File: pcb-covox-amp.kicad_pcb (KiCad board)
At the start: 2 copper layers, 80 x 56 mm, 41 parts, among them J1 DB25, P1 USB, U1 LM386, X1 Amp, X2 Raw

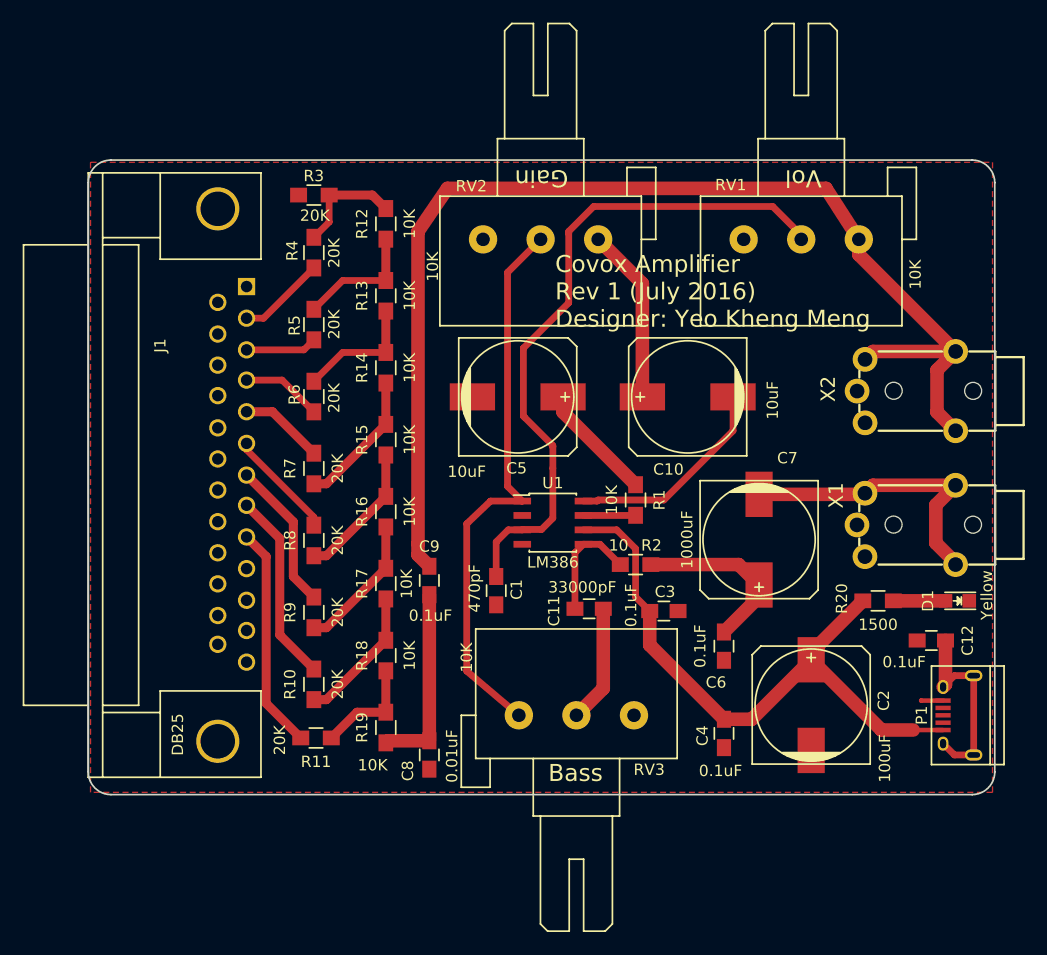
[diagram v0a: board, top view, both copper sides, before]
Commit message: add mounting holes rev 2
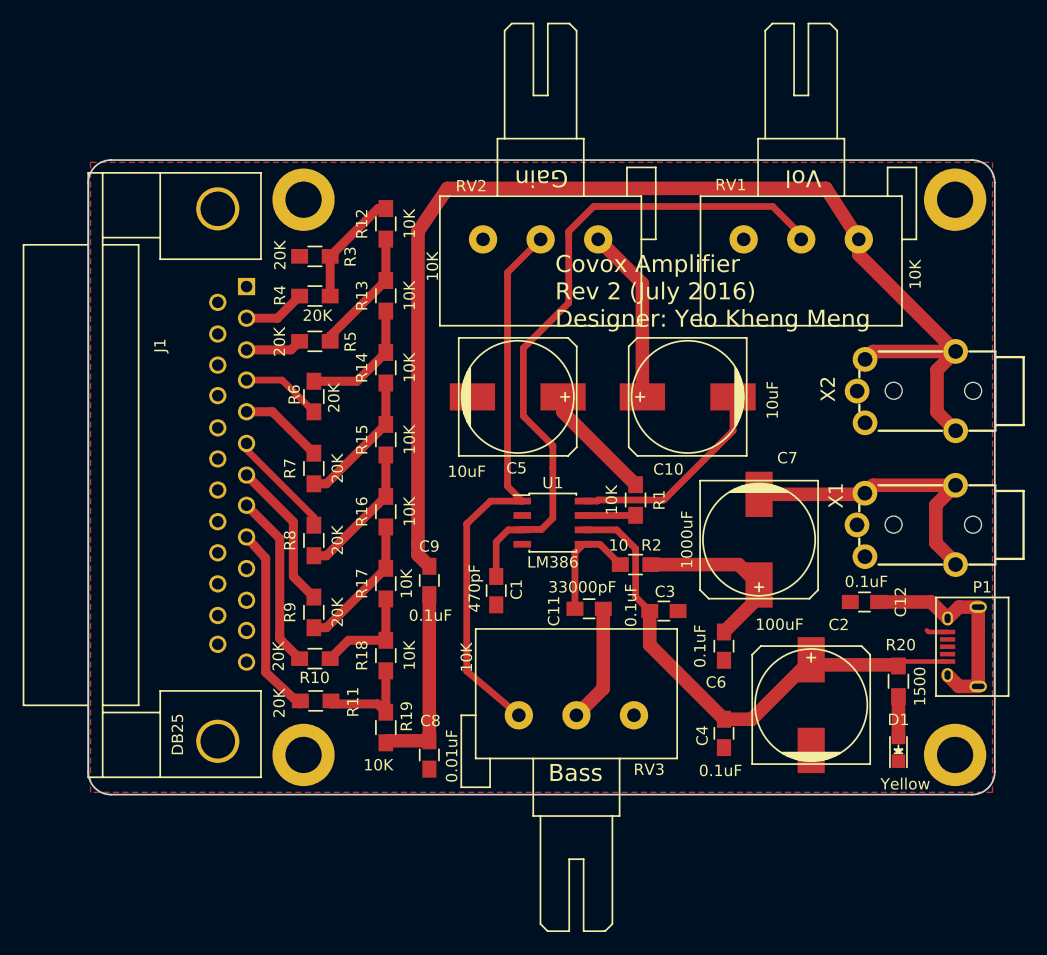
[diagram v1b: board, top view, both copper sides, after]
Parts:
- added MH1: MOUNTHOLE, Mounting_Holes:MountingHole_3.2mm_M3_ISO14580_Pad, F.Cu at (176.5, 89.5)
- added MH2: MOUNTHOLE, Mounting_Holes:MountingHole_3.2mm_M3_ISO14580_Pad, F.Cu at (176.5, 138.5)
- added MH3: MOUNTHOLE, Mounting_Holes:MountingHole_3.2mm_M3_ISO14580_Pad, F.Cu at (119.0, 138.5)
- added MH4: MOUNTHOLE, Mounting_Holes:MountingHole_3.2mm_M3_ISO14580_Pad, F.Cu at (119.0, 89.5)
- moved D1 14.1 mm to (171.5, 138.0), turned to 90 degrees
- moved R20 7.32 mm to (171.5, 132.0), turned to 270 degrees
- moved C12 6.81 mm to (168.5, 125.0)
- moved P1 6.06 mm to (177.4, 128.9)
- moved R3 5.41 mm to (120.0, 94.5)
- moved R4 3.83 mm to (120.0, 98.0), turned to 180 degrees
- moved R11 3.27 mm to (120.1, 133.7)
- moved R10 2.27 mm to (120.0, 130.0), turned to 180 degrees
- moved R5 1.48 mm to (120.0, 102.0), turned to 180 degrees
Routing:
- net +5V: track 54.7 -> 46.4 mm
- net Data7: track 19.7 -> 16.7 mm
- net Net-(R10-Pad1): track 12.2 -> 9.23 mm
- net Net-(C12-Pad2): track 17.6 -> 19.9 mm
- net Data0: track 7.78 -> 5.49 mm
- net Data6: track 16.9 -> 15.5 mm
- net Data1: track 6.30 -> 4.99 mm
- net Net-(D1-Pad2): track 4.60 -> 3.60 mm
- net Net-(R11-Pad1): track 9.40 -> 8.86 mm
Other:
- net class Default: trace_width 1.2 -> 0.4
- board text added: "Covox Amplifier Rev 2 (July 2016) Designer: Yeo Kheng Meng"
- board text removed: "Covox Amplifier Rev 1 (July 2016) Designer: Yeo Kheng Meng"

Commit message: update db25 package
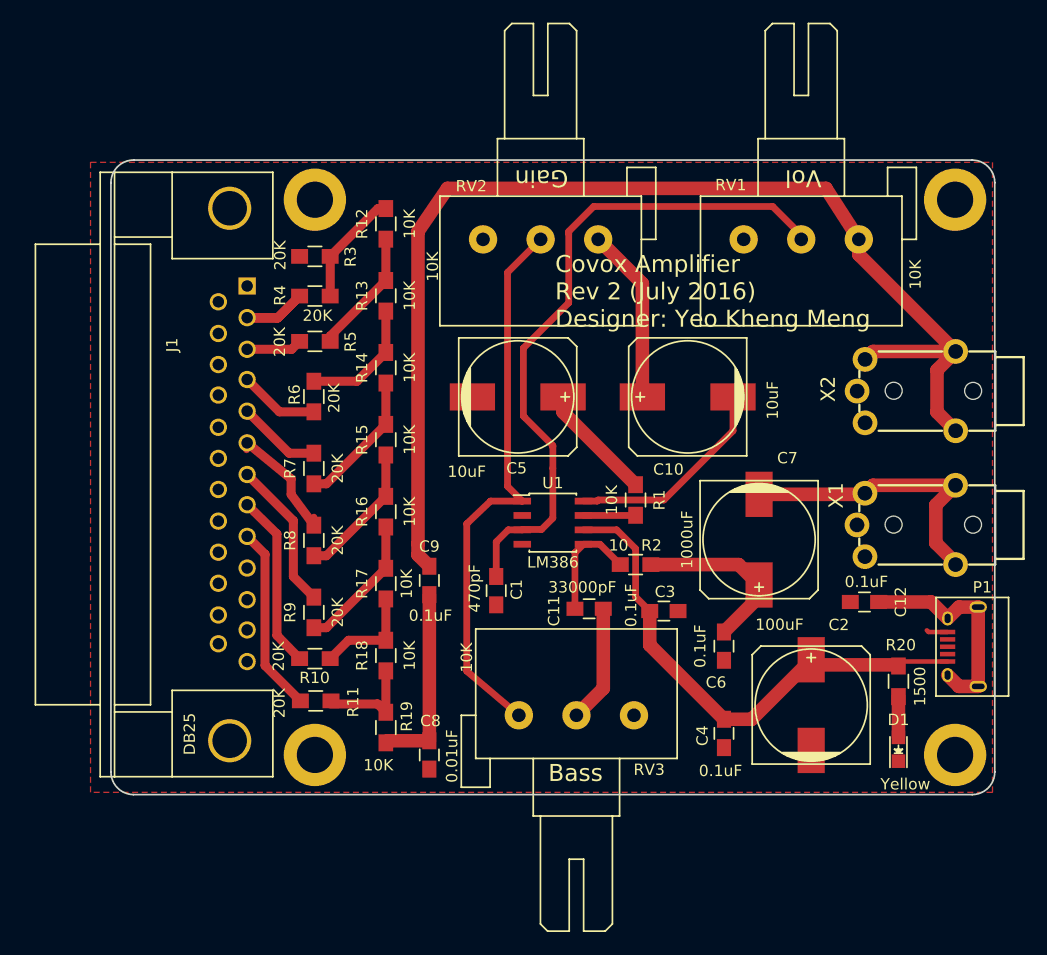
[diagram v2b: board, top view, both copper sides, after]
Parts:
- J1: footprint Connect:DB25MC -> db25:DB25MC
- moved J1 1.05 mm to (113.8, 113.8)
- moved MH3 1.00 mm to (120.0, 138.5)
- moved MH4 1.00 mm to (120.0, 89.5)
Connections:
- J1 pad 1: Net-(J1-Pad1) -> (no net)
- J1 pad 10: Net-(J1-Pad10) -> (no net)
- J1 pad 11: Net-(J1-Pad11) -> (no net)
- J1 pad 12: Net-(J1-Pad12) -> (no net)
- J1 pad 13: Net-(J1-Pad13) -> (no net)
- J1 pad 14: Net-(J1-Pad14) -> (no net)
- J1 pad 15: Net-(J1-Pad15) -> (no net)
- J1 pad 16: Net-(J1-Pad16) -> (no net)
- J1 pad 17: Net-(J1-Pad17) -> (no net)
- J1 pad 18: Net-(J1-Pad18) -> (no net)
- J1 pad 20: Net-(J1-Pad20) -> (no net)
- J1 pad 21: Net-(J1-Pad21) -> (no net)
- J1 pad 22: Net-(J1-Pad22) -> (no net)
- J1 pad 23: Net-(J1-Pad23) -> (no net)
- J1 pad 24: Net-(J1-Pad24) -> (no net)
- J1 pad 25: Net-(J1-Pad25) -> (no net)
- MH1 pad 1: Net-(MH1-Pad1) -> (no net)
- MH2 pad 1: Net-(MH2-Pad1) -> (no net)
- MH3 pad 1: Net-(MH3-Pad1) -> (no net)
- MH4 pad 1: Net-(MH4-Pad1) -> (no net)
- P1 pad 2: Net-(P1-Pad2) -> (no net)
- P1 pad 3: Net-(P1-Pad3) -> (no net)
- P1 pad 4: Net-(P1-Pad4) -> (no net)
- RV2 pad 3: Net-(RV2-Pad3) -> (no net)
- RV3 pad 3: Net-(RV3-Pad3) -> (no net)
- X1 pad P$1: Net-(X1-PadP$1) -> (no net)
- X2 pad P$1: Net-(X2-PadP$1) -> (no net)
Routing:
- net Data0: track 5.49 -> 10.9 mm
- net Data4: track 9.67 -> 11.0 mm
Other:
- board size 80 x 56 mm -> 78 x 56 mm
- net class Default: trace_width 0.4 -> 0.8
